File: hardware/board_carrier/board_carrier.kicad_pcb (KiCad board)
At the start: 2 copper layers, 40 x 36.5 mm, 21 parts, among them J1 Conn_01x08, J2 Conn_01x08, J3 Conn_02x06_Top_Bottom, U1 TJA1051T-3, U2 LM78M05_TO252

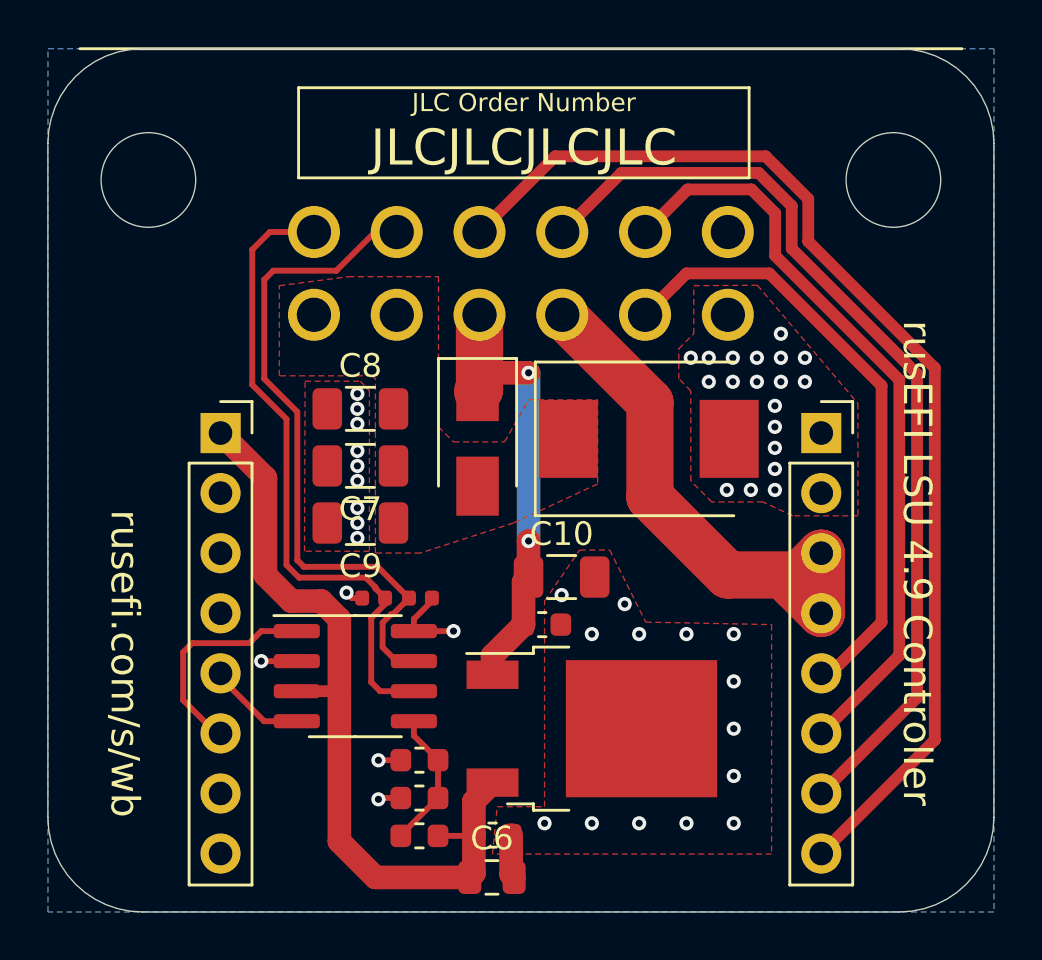
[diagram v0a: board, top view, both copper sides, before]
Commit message: reroute carrier for proper footprint
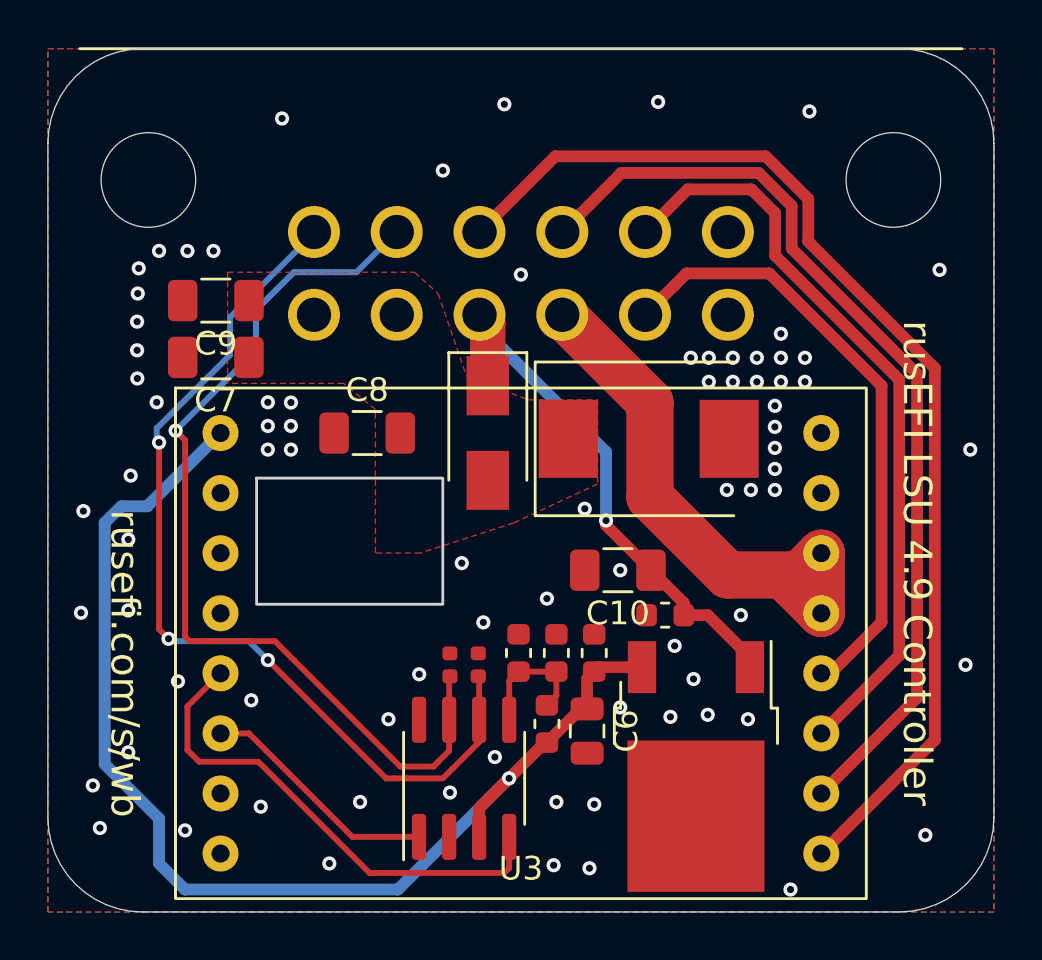
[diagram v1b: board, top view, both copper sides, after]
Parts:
- removed J1, J2: Conn_01x08, Connector_PinSocket_2.54mm:PinSocket_1x08_P2.54mm_Vertical
- removed JLCTAG**: JLC_PCB_TAG, rusefi:JLC_PCB_TAG
- removed REF**: OSHW-Logo_11.4x12mm_SilkScreen, Symbol:OSHW-Logo_11.4x12mm_SilkScreen
- added U3: f042_wideband_module, wideband_module:f042_wideband_module, F.Cu at (47.3, 71.0)
- moved C9 11.2 mm to (47.1, 65.4)
- moved C2 8.82 mm to (63.1, 80.3), turned to 90 degrees
- moved C7 7.64 mm to (47.1, 67.8)
- moved C3 7.43 mm to (59.9, 80.3), turned to 90 degrees
- moved C6 7.38 mm to (62.8, 83.6), turned to -90 degrees
- moved R2 7.35 mm to (61.5, 80.3), turned to 90 degrees
- moved R1 7.17 mm to (61.1, 83.3), turned to 90 degrees
- moved U1 6.31 mm to (57.6, 85.6), turned to 90 degrees
- moved C5 5.25 mm to (58.2, 80.8), turned to 90 degrees
- moved C1 5.22 mm to (66.1, 78.7), turned to 180 degrees
- moved U2 4.68 mm to (67.4, 85.1), turned to -90 degrees
- moved C4 3.09 mm to (57.0, 80.8), turned to -90 degrees
- moved C10 2.40 mm to (64.1, 76.8), turned to 180 degrees
- moved C8 1.06 mm to (53.5, 71.0)
- moved D2 0.50 mm to (58.6, 71.0)
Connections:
- J3 pad 5: (no net) -> unconnected-(J3-Pad5)
- J3 pad 7: (no net) -> unconnected-(J3-Pad7)
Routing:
- net /CAN_RX: track 4.17 -> 21.0 mm
- net +5V: track 34.0 -> 50.3 mm, vias 0 -> 1
- net /CAN_L: track 27.4 -> 39.2 mm, vias 0 -> 3
- net /CAN_H: track 28.4 -> 39.6 mm, vias 0 -> 1
- net GND: track 9.40 -> 0.00 mm, vias 47 -> 79
- net /LSU_Heater+: track 19.6 -> 23.4 mm, vias 2 -> 1
- net /CAN_TX: track 9.37 -> 10.2 mm
- net Net-(C3-Pad1): track 5.92 -> 5.39 mm
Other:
- net class Default removed

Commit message: vbatt sense
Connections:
- U3 pad 7: /nRESET -> /LSU_Heater+
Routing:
- net /LSU_Heater+: track 23.4 -> 44.5 mm, vias 1 -> 2
- net GND: vias 79 -> 85
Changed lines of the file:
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@@
   (net 17 "unconnected-(U3-Pad3)")
   (net 18 "unconnected-(U3-Pad4)")
-  (net 19 "/nRESET")
-  (net 20 "/Boot0")
+  (net 19 "/Boot0")
   (footprint "mx120:mx120g-12" locked (layer "F.Cu")
     (at 60 66)
@@
       (net 8 "/CAN_TX") (pinfunction "CAN_TX") (pintype "output"))
     (pad "7" thru_hole circle (at 0 15.24) (size 1.524 1.524) (drill 0.762) (layers *.Cu *.Mask)
-      (net 19 "/nRESET") (pinfunction "nRESET") (pintype "input"))
+      (net 9 "/LSU_Heater+") (pinfunction "VBatt_Sense") (pintype "input"))
     (pad "8" thru_hole circle (at 0 17.78) (size 1.524 1.524) (drill 0.762) (layers *.Cu *.Mask)
-      (net 20 "/Boot0") (pinfunction "Boot0") (pintype "input"))
+      (net 19 "/Boot0") (pinfunction "Boot0") (pintype "input"))
     (pad "9" thru_hole circle (at 25.4 0) (size 1.524 1.524) (drill 0.762) (layers *.Cu *.Mask)
       (net 1 "GND") (pinfunction "HEAT_GND") (pintype "power_in"))
@@
   (via (at 68.707 73.406) (size 0.6) (drill 0.3) (layers "F.Cu" "B.Cu") (net 1))
   (via (at 67.183 67.818) (size 0.6) (drill 0.3) (layers "F.Cu" "B.Cu") (net 1))
+  (via (at 50.8 84) (size 0.6) (drill 0.3) (layers "F.Cu" "B.Cu") (net 1))
   (via (at 41.5 74.3) (size 0.6) (drill 0.3) (layers "F.Cu" "B.Cu") (net 1))
   (via (at 65.8 57) (size 0.6) (drill 0.3) (layers "F.Cu" "B.Cu") (net 1))
   (via (at 43.4 75.5) (size 0.6) (drill 0.3) (layers "F.Cu" "B.Cu") (net 1))
+  (via (at 54.9 79.7) (size 0.6) (drill 0.3) (layers "F.Cu" "B.Cu") (net 1))
   (via (at 72.2 57.4) (size 0.6) (drill 0.3) (layers "F.Cu" "B.Cu") (net 1))
   (via (at 49.3 69.7) (size 0.6) (drill 0.3) (layers "F.Cu" "B.Cu") (net 1))
   (via (at 43.8 65.1) (size 0.6) (drill 0.3) (layers "F.Cu" "B.Cu") (net 1))
+  (via (at 59.4 77.5) (size 0.6) (drill 0.3) (layers "F.Cu" "B.Cu") (net 1))
   (via (at 49.3 70.7) (size 0.6) (drill 0.3) (layers "F.Cu" "B.Cu") (net 1))
   (via (at 78.8 80.8) (size 0.6) (drill 0.3) (layers "F.Cu" "B.Cu") (net 1))
@@
   (via (at 59.3 57.1) (size 0.6) (drill 0.3) (layers "F.Cu" "B.Cu") (net 1))
   (via (at 61.5 86.6) (size 0.6) (drill 0.3) (layers "F.Cu" "B.Cu") (net 1))
+  (via (at 53 79.1) (size 0.6) (drill 0.3) (layers "F.Cu" "B.Cu") (net 1))
   (via (at 49.3 71.7) (size 0.6) (drill 0.3) (layers "F.Cu" "B.Cu") (net 1))
   (via (at 45.5 81.5) (size 0.6) (drill 0.3) (layers "F.Cu" "B.Cu") (net 1))
   (via (at 69.3 78.7) (size 0.6) (drill 0.3) (layers "F.Cu" "B.Cu") (net 1))
+  (via (at 51.7 80.6) (size 0.6) (drill 0.3) (layers "F.Cu" "B.Cu") (net 1))
   (via (at 45.9 63.3) (size 0.6) (drill 0.3) (layers "F.Cu" "B.Cu") (net 1))
   (via (at 43.781879 68.691948) (size 0.6) (drill 0.3) (layers "F.Cu" "B.Cu") (net 1))
@@
   (via (at 53.2 86.6) (size 0.6) (drill 0.3) (layers "F.Cu" "B.Cu") (net 1))
   (via (at 44.7 63.3) (size 0.6) (drill 0.3) (layers "F.Cu" "B.Cu") (net 1))
-  (via (at 62.7 74.2) (size 0.6) (drill 0.3) (layers "F.Cu" "B.Cu") (net 1))
+  (via (at 62.8 74) (size 0.6) (drill 0.3) (layers "F.Cu" "B.Cu") (net 1))
   (via (at 43.841189 64.036122) (size 0.6) (drill 0.3) (layers "F.Cu" "B.Cu") (net 1))
   (via (at 69.6 83.1) (size 0.6) (drill 0.3) (layers "F.Cu" "B.Cu") (net 1))
@@
   (via (at 50.276312 71.7) (size 0.6) (drill 0.3) (layers "F.Cu" "B.Cu") (net 1))
   (via (at 64.2 82.6) (size 0.6) (drill 0.3) (layers "F.Cu" "B.Cu") (net 1))
+  (via (at 53 81.8) (size 0.6) (drill 0.3) (layers "F.Cu" "B.Cu") (net 1))
   (via (at 67.3 81.4) (size 0.6) (drill 0.3) (layers "F.Cu" "B.Cu") (net 1))
   (via (at 51.9 89.2) (size 0.6) (drill 0.3) (layers "F.Cu" "B.Cu") (net 1))
@@
   (segment (start 48.5 83.7) (end 52.875 88.075) (width 0.25) (layer "F.Cu") (net 8))
   (segment (start 52.875 88.075) (end 55.695 88.075) (width 0.25) (layer "F.Cu") (net 8))
+  (segment (start 56.9 78.8) (end 61 74.7) (width 0.2) (layer "F.Cu") (net 9))
   (segment (start 69.68 80.48) (end 67.9 78.7) (width 0.5) (layer "F.Cu") (net 9))
+  (segment (start 52.7 80.8) (end 54.7 78.8) (width 0.2) (layer "F.Cu") (net 9))
   (segment (start 65.5 76.8) (end 66.8875 78.1875) (width 0.5) (layer "F.Cu") (net 9))
   (segment (start 58.25 66) (end 58.6 66.35) (width 1.5) (layer "F.Cu") (net 9))
@@
   (segment (start 67.9 78.7) (end 66.8875 78.7) (width 0.5) (layer "F.Cu") (net 9))
   (segment (start 63.6 74.9) (end 65.5 76.8) (width 0.5) (layer "F.Cu") (net 9))
+  (segment (start 54.7 78.8) (end 56.9 78.8) (width 0.2) (layer "F.Cu") (net 9))
+  (segment (start 61 74.7) (end 63.6 74.7) (width 0.2) (layer "F.Cu") (net 9))
+  (via (at 52.7 80.8) (size 0.6) (drill 0.3) (layers "F.Cu" "B.Cu") (net 9))
   (via (at 63.6 74.7) (size 0.6) (drill 0.3) (layers "F.Cu" "B.Cu") (net 9))
+  (segment (start 47.3 86.2) (end 52.7 80.8) (width 0.2) (layer "B.Cu") (net 9))
   (segment (start 60.3 68.5) (end 63.6 71.8) (width 0.5) (layer "B.Cu") (net 9))
+  (segment (start 47.3 86.24) (end 47.3 86.2) (width 0.2) (layer "B.Cu") (net 9))
   (segment (start 63.6 71.8) (end 63.6 74.7) (width 0.5) (layer "B.Cu") (net 9))
   (segment (start 58.25 66) (end 58.25 66.45) (width 0.5) (layer "B.Cu") (net 9))
